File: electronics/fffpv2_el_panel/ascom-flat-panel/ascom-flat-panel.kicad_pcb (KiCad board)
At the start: 2 copper layers, 55 x 46.6 mm, 19 parts, among them J1 Servo, Q1 IRLZ34N, Q2 IRLZ34N, U1 XIAO-SAMD21-DIP, U2 TLC272

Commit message: ajout d'une empreinte pour le connecteur JST en direction de l'inverter. Je laisse le pro du routage câbler ça j'ai peur de tout péter :D
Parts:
- added J2: Conn_01x02, Connector_JST:JST_XH_B2B-XH-A_1x02_P2.50mm_Vertical, F.Cu at (118.0, 101.5)
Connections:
- U1 pad 12: +3V3 -> unconnected-(U1-3V3-Pad12)

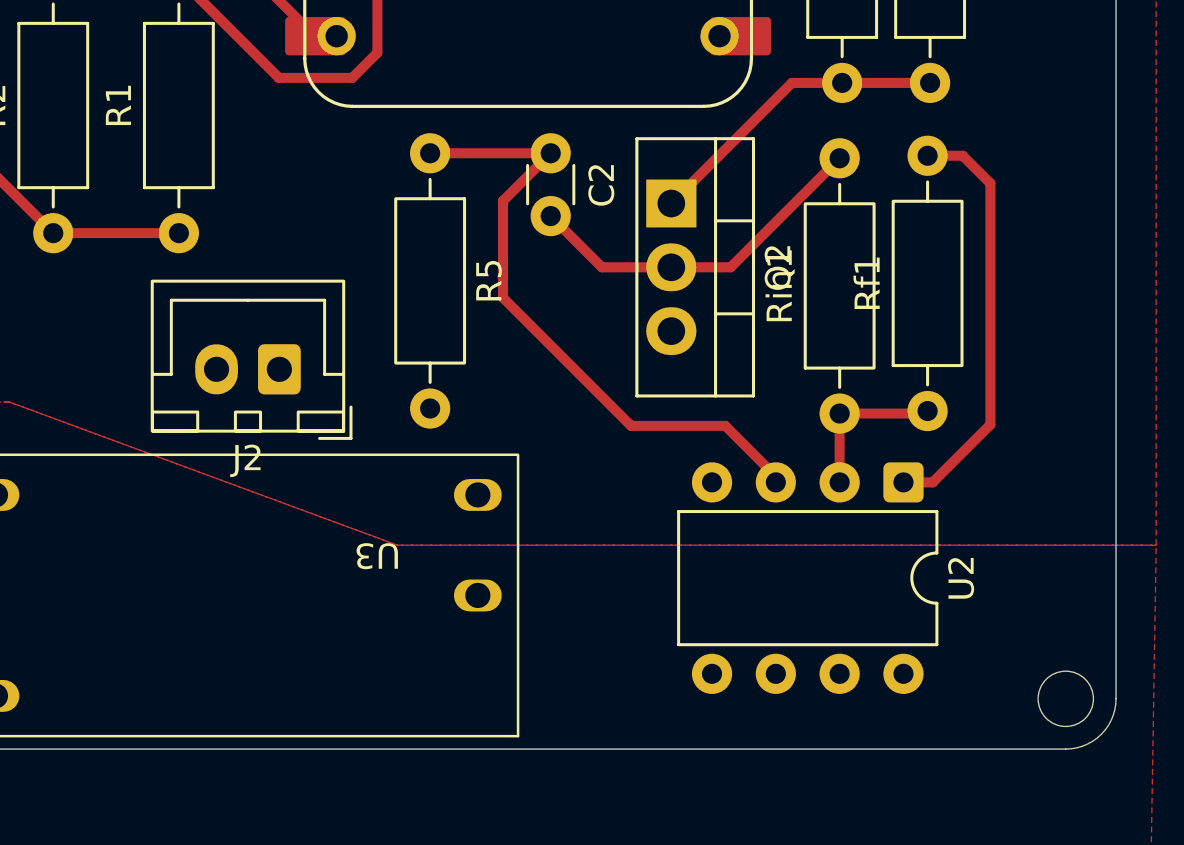
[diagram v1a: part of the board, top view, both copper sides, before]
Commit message: Routing 2 pin connector
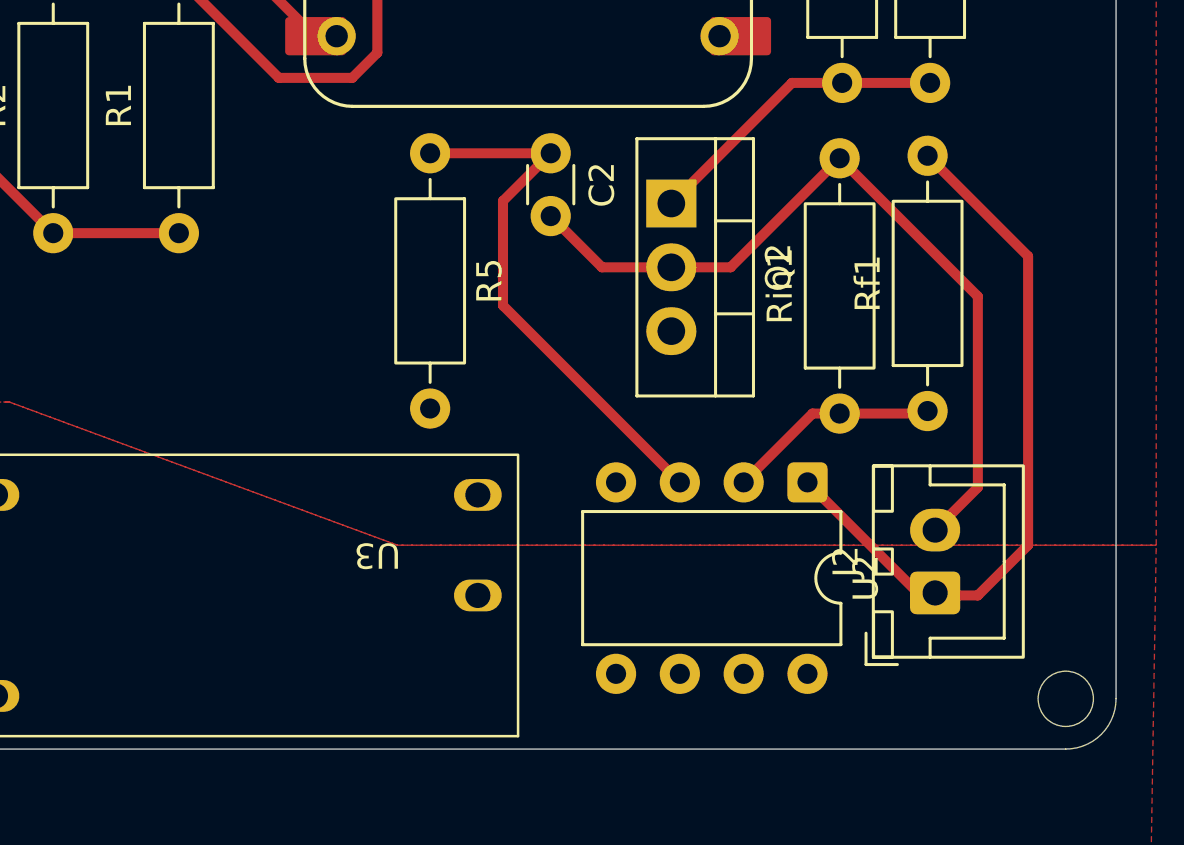
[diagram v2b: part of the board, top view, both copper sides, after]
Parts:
- moved J2 27.6 mm to (144.1, 110.4), turned to 90 degrees
- moved U2 3.82 mm to (139.0, 106.0)
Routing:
- net EL PANEL CONTROL CIRCUIT: track 14.1 -> 31.9 mm
- net EL_DRIVER+: track 17.0 -> 28.6 mm
- net Net-(U2A-+): track 25.4 -> 21.6 mm
- net Net-(U2A--): track 6.28 -> 8.50 mm
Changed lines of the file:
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@@
 	(footprint "Connector_JST:JST_XH_B2B-XH-A_1x02_P2.50mm_Vertical"
 		(layer "F.Cu")
-		(at 118 101.5 180)
+		(at 144.1 110.4 90)
 		(descr "JST XH series connector, B2B-XH-A (http://www.jst-mfg.com/product/pdf/eng/eXH.pdf), generated with kicad-footprint-generator")
 		(tags "connector JST XH vertical")
 		(property "Reference" "J2"
-			(at 1.25 -3.55 0)
+			(at 1.25 -3.55 90)
 			(layer "F.SilkS")
 			(effects
@@
 		)
 		(property "Value" "Conn_01x02"
-			(at 1.25 4.6 0)
+			(at 1.25 4.6 90)
 			(layer "F.Fab")
 			(effects
@@
 		)
 		(property "Datasheet" "~"
-			(at 0 0 0)
+			(at 0 0 90)
 			(layer "F.Fab")
 			(hide yes)
@@
 		)
 		(property "Description" "Generic connector, single row, 01x02, script generated (kicad-library-utils/schlib/autogen/connector/)"
-			(at 0 0 0)
+			(at 0 0 90)
 			(layer "F.Fab")
 			(hide yes)
@@
 		(attr through_hole)
 		(fp_line
-			(start 5.05 -0.2)
-			(end 4.3 -0.2)
+			(start -1.6 -2.75)
+			(end -2.85 -2.75)
 			(stroke
 				(width 0.12)
@@
 		)
 		(fp_line
-			(start 4.3 2.75)
-			(end 1.25 2.75)
+			(start -2.85 -2.75)
+			(end -2.85 -1.5)
 			(stroke
 				(width 0.12)
@@
 		)
 		(fp_line
-			(start 4.3 -0.2)
-			(end 4.3 2.75)
+			(start 5.05 -0.2)
+			(end 4.3 -0.2)
 			(stroke
 				(width 0.12)
@@
 		)
 		(fp_line
-			(start -1.6 -2.75)
-			(end -2.85 -2.75)
+			(start 4.3 -0.2)
+			(end 4.3 2.75)
 			(stroke
 				(width 0.12)
@@
 		)
 		(fp_line
-			(start -1.8 2.75)
-			(end 1.25 2.75)
+			(start -1.8 -0.2)
+			(end -1.8 2.75)
 			(stroke
 				(width 0.12)
@@
 		)
 		(fp_line
-			(start -1.8 -0.2)
-			(end -1.8 2.75)
+			(start -2.55 -0.2)
+			(end -1.8 -0.2)
 			(stroke
 				(width 0.12)
@@
 		)
 		(fp_line
-			(start -2.55 -0.2)
-			(end -1.8 -0.2)
+			(start 4.3 2.75)
+			(end 1.25 2.75)
 			(stroke
 				(width 0.12)
@@
 		)
 		(fp_line
-			(start -2.85 -2.75)
-			(end -2.85 -1.5)
+			(start -1.8 2.75)
+			(end 1.25 2.75)
 			(stroke
 				(width 0.12)
@@
 		)
 		(fp_rect
-			(start 3.25 -2.45)
-			(end 5.05 -1.7)
+			(start -2.56 -2.46)
+			(end 5.06 3.51)
 			(stroke
 				(width 0.12)
@@
 		)
 		(fp_rect
-			(start 0.75 -2.45)
-			(end 1.75 -1.7)
+			(start 3.25 -2.45)
+			(end 5.05 -1.7)
 			(stroke
 				(width 0.12)
@@
 		)
 		(fp_rect
-			(start -2.55 -2.45)
-			(end -0.75 -1.7)
+			(start 0.75 -2.45)
+			(end 1.75 -1.7)
 			(stroke
 				(width 0.12)
@@
 		)
 		(fp_rect
-			(start -2.56 -2.46)
-			(end 5.06 3.51)
+			(start -2.55 -2.45)
+			(end -0.75 -1.7)
 			(stroke
 				(width 0.12)
@@
 		)
 		(fp_line
-			(start 0 -1.35)
-			(end 0.625 -2.35)
+			(start -0.625 -2.35)
+			(end 0 -1.35)
 			(stroke
 				(width 0.1)
@@
 		)
 		(fp_line
-			(start -0.625 -2.35)
-			(end 0 -1.35)
+			(start 0 -1.35)
+			(end 0.625 -2.35)
 			(stroke
 				(width 0.1)
@@
 		)
 		(fp_text user "${REFERENCE}"
-			(at 1.25 2.7 0)
+			(at 1.25 2.7 90)
 			(layer "F.Fab")
 			(effects
@@
 		)
 		(pad "1" thru_hole roundrect
-			(at 0 0 180)
+			(at 0 0 90)
 			(size 1.7 2)
 			(drill 1)
@@
 		)
 		(pad "2" thru_hole oval
-			(at 2.5 0 180)
+			(at 2.5 0 90)
 			(size 1.7 2)
 			(drill 1)
@@
 	(footprint "Package_DIP:DIP-8_W7.62mm"
 		(layer "F.Cu")
-		(at 142.84 106 -90)
+		(at 139.02 106 -90)
 		(descr "8-lead though-hole mounted DIP package, row spacing 7.62mm (300 mils)")
 		(tags "THT DIP DIL PDIP 2.54mm 7.62mm 300mil")
@@
 	)
 	(segment
-		(start 137.76 105.76)
-		(end 137.76 106)
+		(start 126.9 94.8)
+		(end 126.9 98.96)
 		(width 0.4)
 		(layer "F.Cu")
@@
 	)
 	(segment
-		(start 132 103.75)
-		(end 135.75 103.75)
+		(start 126.9 98.96)
+		(end 133.94 106)
 		(width 0.4)
 		(layer "F.Cu")
@@
 	)
 	(segment
-		(start 126.9 98.65)
-		(end 132 103.75)
+		(start 128.8 92.9)
+		(end 126.9 94.8)
 		(width 0.4)
 		(layer "F.Cu")
@@
 	)
 	(segment
-		(start 135.75 103.75)
-		(end 137.76 105.76)
+		(start 124 92.9)
+		(end 128.8 92.9)
 		(width 0.4)
 		(layer "F.Cu")
@@
 	)
 	(segment
-		(start 126.9 94.8)
-		(end 126.9 98.65)
+		(start 130.84 97.44)
+		(end 128.8 95.4)
 		(width 0.4)
 		(layer "F.Cu")
-		(net 19)
+		(net 20)
 	)
 	(segment
-		(start 124 92.9)
-		(end 128.8 92.9)
+		(start 145.8 106.2)
+		(end 145.8 98.6)
 		(width 0.4)
 		(layer "F.Cu")
-		(net 19)
+		(net 20)
 	)
 	(segment
-		(start 128.8 92.9)
-		(end 126.9 94.8)
+		(start 145.8 98.6)
+		(end 140.3 93.1)
 		(width 0.4)
 		(layer "F.Cu")
-		(net 19)
+		(net 20)
 	)
 	(segment
-		(start 130.84 97.44)
-		(end 128.8 95.4)
+		(start 144.1 107.9)
+		(end 145.8 106.2)
 		(width 0.4)
 		(layer "F.Cu")
@@
 	)
 	(segment
-		(start 145.2 93)
-		(end 146.3 94.1)
+		(start 144.1 110.4)
+		(end 144.2 110.5)
 		(width 0.4)
 		(layer "F.Cu")
@@
 	)
 	(segment
-		(start 146.3 94.1)
-		(end 146.3 103.7)
+		(start 147.8 108.5)
+		(end 147.8 97)
 		(width 0.4)
 		(layer "F.Cu")
@@
 	)
 	(segment
-		(start 146.3 103.7)
-		(end 144 106)
+		(start 144.2 110.5)
+		(end 145.8 110.5)
 		(width 0.4)
 		(layer "F.Cu")
@@
 	)
 	(segment
-		(start 143.8 93)
-		(end 145.2 93)
+		(start 143.42 110.4)
+		(end 139.02 106)
 		(width 0.4)
 		(layer "F.Cu")
@@
 	)
 	(segment
-		(start 144 106)
-		(end 142.84 106)
+		(start 145.8 110.5)
+		(end 147.8 108.5)
 		(width 0.4)
 		(layer "F.Cu")
@@
 	)
 	(segment
+		(start 147.8 97)
+		(end 143.8 93)
+		(width 0.4)
+		(layer "F.Cu")
+		(net 22)
+	)
+	(segment
+		(start 144.1 110.4)
+		(end 143.42 110.4)
+		(width 0.4)
+		(layer "F.Cu")
+		(net 22)
+	)
+	(segment
+		(start 139.22 103.26)
+		(end 140.3 103.26)
+		(width 0.4)
+		(layer "F.Cu")
+		(net 23)
+	)
+	(segment
 		(start 143.7 103.26)
 		(end 143.8 103.16)
@@
 	)
 	(segment
-		(start 140.3 103.26)
-		(end 140.3 106)
+		(start 136.48 106)
+		(end 139.22 103.26)
 		(width 0.4)
 		(layer "F.Cu")

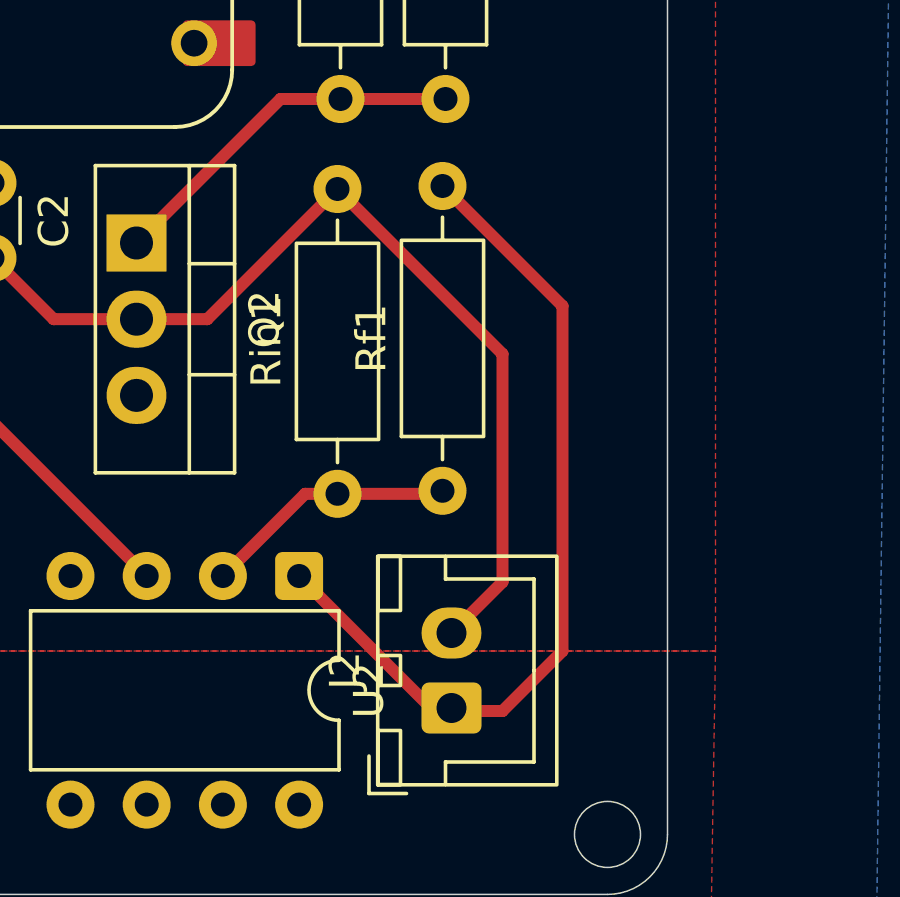
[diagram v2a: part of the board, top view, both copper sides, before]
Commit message: EL driver '-' pin should be grounded
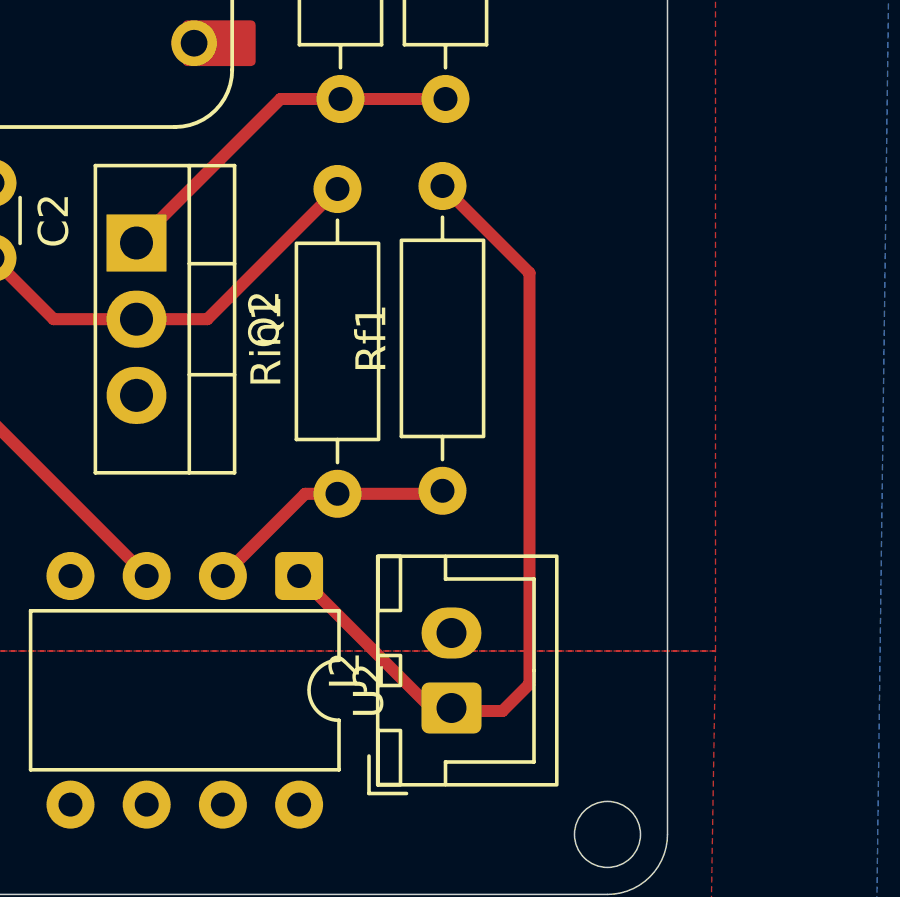
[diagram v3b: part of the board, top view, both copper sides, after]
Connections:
- J2 pad 2: EL PANEL CONTROL CIRCUIT -> GND
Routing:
- net EL PANEL CONTROL CIRCUIT: track 31.9 -> 14.1 mm
- net EL_DRIVER+: track 28.6 -> 27.7 mm
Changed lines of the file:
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@@
 			(layers "*.Cu" "*.Mask")
 			(remove_unused_layers no)
-			(net 20 "EL PANEL CONTROL CIRCUIT")
+			(net 1 "GND")
 			(pinfunction "Pin_2")
 			(pintype "passive")
@@
 	)
 	(segment
-		(start 145.8 106.2)
-		(end 145.8 98.6)
-		(width 0.4)
-		(layer "F.Cu")
-		(net 20)
-	)
-	(segment
-		(start 145.8 98.6)
-		(end 140.3 93.1)
-		(width 0.4)
-		(layer "F.Cu")
-		(net 20)
-	)
-	(segment
-		(start 144.1 107.9)
-		(end 145.8 106.2)
-		(width 0.4)
-		(layer "F.Cu")
-		(net 20)
-	)
-	(segment
 		(start 133.6 97.44)
 		(end 135.96 97.44)
@@
 	)
 	(segment
-		(start 144.1 110.4)
-		(end 144.2 110.5)
+		(start 145.8 110.5)
+		(end 146.7 109.6)
 		(width 0.4)
 		(layer "F.Cu")
@@
 	)
 	(segment
-		(start 147.8 108.5)
-		(end 147.8 97)
+		(start 146.7 109.6)
+		(end 146.7 95.9)
 		(width 0.4)
 		(layer "F.Cu")
@@
 	)
 	(segment
-		(start 144.2 110.5)
-		(end 145.8 110.5)
+		(start 143.42 110.4)
+		(end 139.02 106)
 		(width 0.4)
 		(layer "F.Cu")
@@
 	)
 	(segment
-		(start 143.42 110.4)
-		(end 139.02 106)
+		(start 144.2 110.5)
+		(end 145.8 110.5)
 		(width 0.4)
 		(layer "F.Cu")
@@
 	)
 	(segment
-		(start 145.8 110.5)
-		(end 147.8 108.5)
+		(start 144.1 110.4)
+		(end 144.2 110.5)
 		(width 0.4)
 		(layer "F.Cu")
@@
 	)
 	(segment
-		(start 147.8 97)
+		(start 146.7 95.9)
 		(end 143.8 93)
 		(width 0.4)

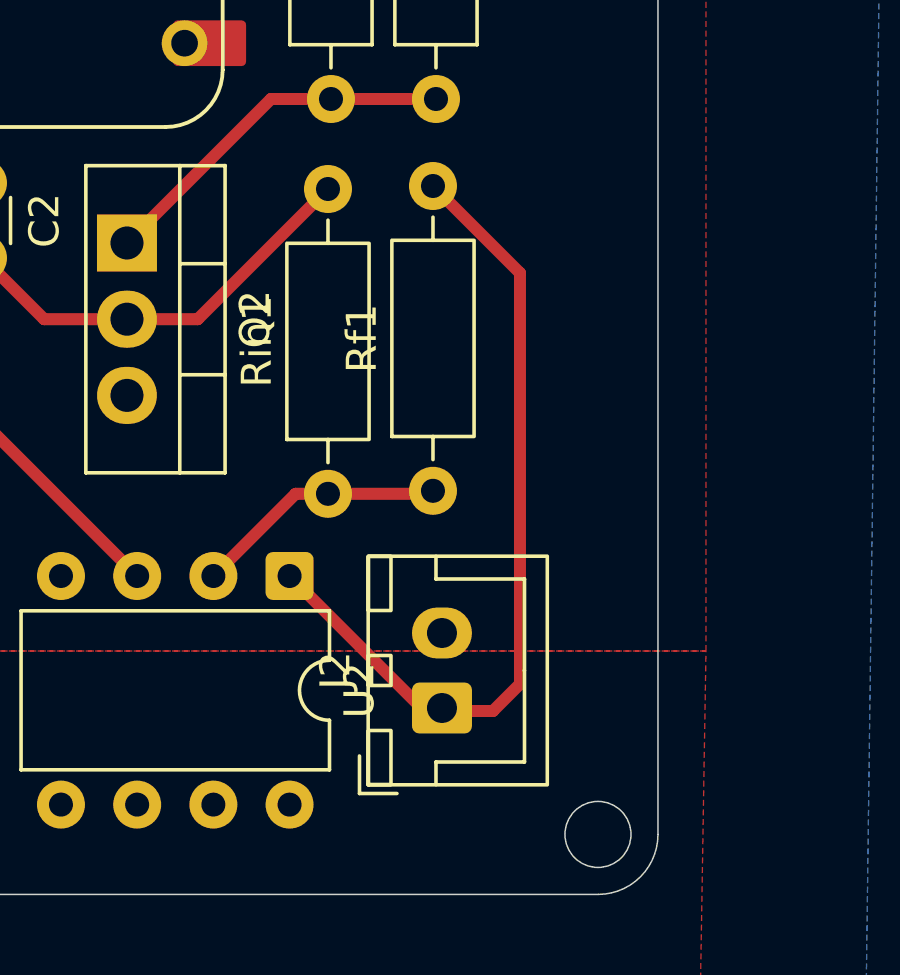
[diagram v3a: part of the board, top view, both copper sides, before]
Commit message: Flip connector for shorter traces and rearanged schematics
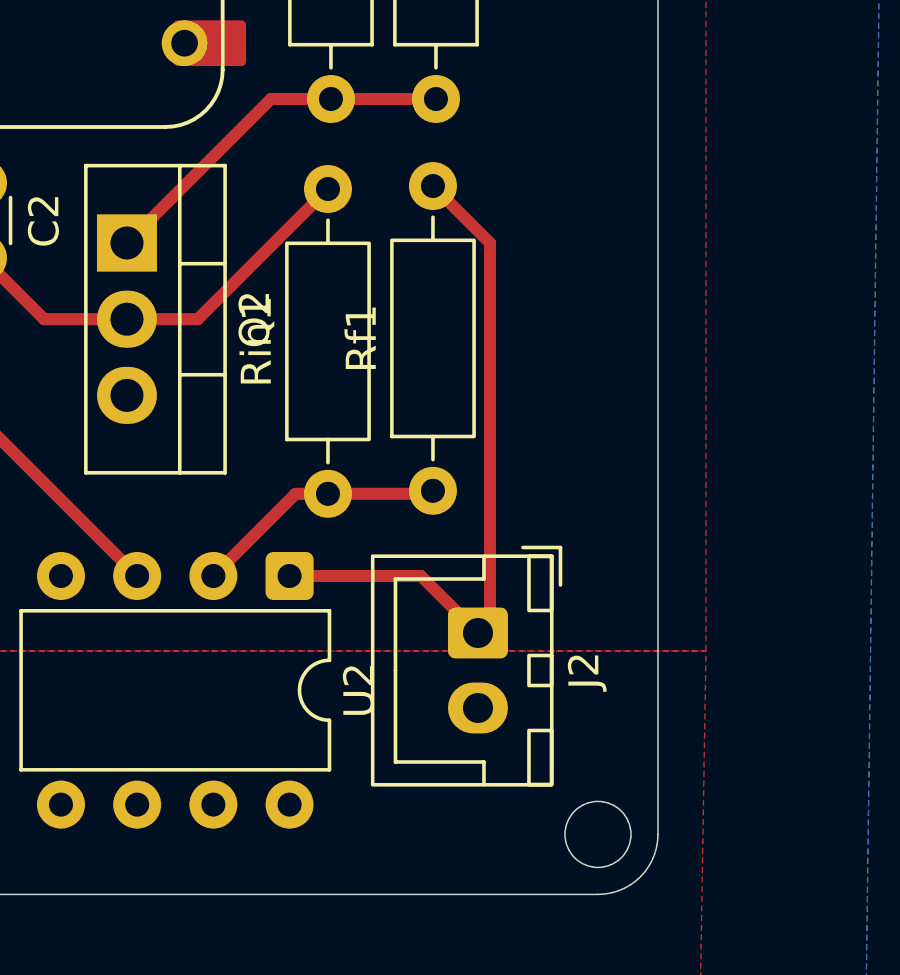
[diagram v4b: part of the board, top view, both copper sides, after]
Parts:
- moved J2 2.77 mm to (145.3, 107.9), turned to -90 degrees
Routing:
- net EL_DRIVER+: track 27.7 -> 22.9 mm
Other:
- board text added: "FFFPV2"
- board text removed: "FFFPV1"
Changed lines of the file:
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@@
 	(footprint "Connector_JST:JST_XH_B2B-XH-A_1x02_P2.50mm_Vertical"
 		(layer "F.Cu")
-		(at 144.1 110.4 90)
+		(at 145.3 107.9 -90)
 		(descr "JST XH series connector, B2B-XH-A (http://www.jst-mfg.com/product/pdf/eng/eXH.pdf), generated with kicad-footprint-generator")
 		(tags "connector JST XH vertical")
@@
 		(attr through_hole)
 		(fp_line
-			(start -1.6 -2.75)
-			(end -2.85 -2.75)
+			(start -1.8 2.75)
+			(end 1.25 2.75)
 			(stroke
 				(width 0.12)
@@
 		)
 		(fp_line
-			(start -2.85 -2.75)
-			(end -2.85 -1.5)
+			(start 4.3 2.75)
+			(end 1.25 2.75)
 			(stroke
 				(width 0.12)
@@
 		)
 		(fp_line
-			(start 5.05 -0.2)
-			(end 4.3 -0.2)
+			(start -2.55 -0.2)
+			(end -1.8 -0.2)
 			(stroke
 				(width 0.12)
@@
 		)
 		(fp_line
-			(start 4.3 -0.2)
-			(end 4.3 2.75)
+			(start -1.8 -0.2)
+			(end -1.8 2.75)
 			(stroke
 				(width 0.12)
@@
 		)
 		(fp_line
-			(start -1.8 -0.2)
-			(end -1.8 2.75)
+			(start 4.3 -0.2)
+			(end 4.3 2.75)
 			(stroke
 				(width 0.12)
@@
 		)
 		(fp_line
-			(start -2.55 -0.2)
-			(end -1.8 -0.2)
+			(start 5.05 -0.2)
+			(end 4.3 -0.2)
 			(stroke
 				(width 0.12)
@@
 		)
 		(fp_line
-			(start 4.3 2.75)
-			(end 1.25 2.75)
+			(start -2.85 -2.75)
+			(end -2.85 -1.5)
 			(stroke
 				(width 0.12)
@@
 		)
 		(fp_line
-			(start -1.8 2.75)
-			(end 1.25 2.75)
+			(start -1.6 -2.75)
+			(end -2.85 -2.75)
 			(stroke
 				(width 0.12)
@@
 		)
 		(fp_rect
-			(start -2.56 -2.46)
-			(end 5.06 3.51)
+			(start -2.55 -2.45)
+			(end -0.75 -1.7)
 			(stroke
 				(width 0.12)
@@
 		)
 		(fp_rect
-			(start 3.25 -2.45)
-			(end 5.05 -1.7)
+			(start 0.75 -2.45)
+			(end 1.75 -1.7)
 			(stroke
 				(width 0.12)
@@
 		)
 		(fp_rect
-			(start 0.75 -2.45)
-			(end 1.75 -1.7)
+			(start 3.25 -2.45)
+			(end 5.05 -1.7)
 			(stroke
 				(width 0.12)
@@
 		)
 		(fp_rect
-			(start -2.55 -2.45)
-			(end -0.75 -1.7)
+			(start -2.56 -2.46)
+			(end 5.06 3.51)
 			(stroke
 				(width 0.12)
@@
 		)
 		(fp_line
-			(start -0.625 -2.35)
-			(end 0 -1.35)
+			(start 0 -1.35)
+			(end 0.625 -2.35)
 			(stroke
 				(width 0.1)
@@
 		)
 		(fp_line
-			(start 0 -1.35)
-			(end 0.625 -2.35)
+			(start -0.625 -2.35)
+			(end 0 -1.35)
 			(stroke
 				(width 0.1)
@@
 		)
 		(pad "1" thru_hole roundrect
-			(at 0 0 90)
+			(at 0 0 270)
 			(size 1.7 2)
 			(drill 1)
@@
 		)
 		(pad "2" thru_hole oval
-			(at 2.5 0 90)
+			(at 2.5 0 270)
 			(size 1.7 2)
 			(drill 1)
@@
 		)
 	)
-	(gr_text "FFFPV1"
+	(gr_text "FFFPV2"
 		(at 133.35 88.2904 0)
 		(layer "B.SilkS")
@@
 	)
 	(segment
-		(start 145.8 110.5)
-		(end 146.7 109.6)
-		(width 0.4)
-		(layer "F.Cu")
-		(net 22)
-	)
-	(segment
-		(start 146.7 109.6)
-		(end 146.7 95.9)
-		(width 0.4)
-		(layer "F.Cu")
-		(net 22)
-	)
-	(segment
-		(start 143.42 110.4)
-		(end 139.02 106)
+		(start 145.3 107.9)
+		(end 145.7 107.5)
 		(width 0.4)
 		(layer "F.Cu")
@@
 	)
 	(segment
-		(start 144.2 110.5)
-		(end 145.8 110.5)
+		(start 139.02 106)
+		(end 143.4 106)
 		(width 0.4)
 		(layer "F.Cu")
@@
 	)
 	(segment
-		(start 144.1 110.4)
-		(end 144.2 110.5)
+		(start 143.4 106)
+		(end 145.3 107.9)
 		(width 0.4)
 		(layer "F.Cu")
@@
 	)
 	(segment
-		(start 146.7 95.9)
+		(start 145.7 94.9)
 		(end 143.8 93)
 		(width 0.4)
@@
 	)
 	(segment
-		(start 144.1 110.4)
-		(end 143.42 110.4)
+		(start 145.7 107.5)
+		(end 145.7 94.9)
 		(width 0.4)
 		(layer "F.Cu")
